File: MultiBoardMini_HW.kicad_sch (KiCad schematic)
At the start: 54 parts, among them J1 PB0, J2 PA10, J3 Conn_01x02_Male, J4 Conn_01x03, J6 Conn_01x04, SW1 PF1, SW2 RESET, SW3 PF0, SW4 PF1, T1 PTS_1.5_2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

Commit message: update sch
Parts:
- removed R11, R12: 10k, Resistor_SMD:R_0603_1608Metric, symbol Device:R
- SW4: value PF1 -> ~
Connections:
- net at ENC/IO_2.3 (Pin_3), PA2.2 (A), U2.4_7 (PA6): no longer IO_1.4 (Pin_4)
- net at J6.2 (Pin_2), U3.11 (RXD): now also U2.3_1 (PA9); no longer U2.4_5 (PA2)
- net at J6.1 (Pin_1), U3.12 (TXD): now also U2.3_2 (PA10); no longer U2.4_10 (PA3)
- net at SW3.2 (B): now also U2.4_15 (PB3); no longer U2.3_10 (PF0)
- net at U5.22 (PWM): now also U2.3_6 (PB0); no longer U2.3_1 (PA9)
- net at U2.3_12 (PA8): now also U5.8 (IN1); no longer U4.22 (PWM)
- net at U2.3_14 (PB5): now also U5.9 (IN2)
- net at U2.3_15 (PB4): now also U4.8 (IN1)
- net at J2.3 (Pin_3): now also U2.4_10 (PA3); no longer U2.3_2 (PA10)
- net at U2.3_7 (PB7): now also IO_1.4 (Pin_4); no longer U5.9 (IN2)
- net at U2.3_8 (PB6): now also IO_1.3 (Pin_3); no longer U5.8 (IN1)
- net at U2.3_9 (PB1): now also U4.22 (PWM); no longer U4.9 (IN2)
- net at U2.4_8 (PA5): now also U4.9 (IN2); no longer IO_1.3 (Pin_3)
- net at U2.4_9 (PA4): now also J1.3 (Pin_3)
- no-connect marks 8 -> 7
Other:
- moved on the sheet: J1, J2, PA1, PA2, PWR1, R4, R5, R6, SW3

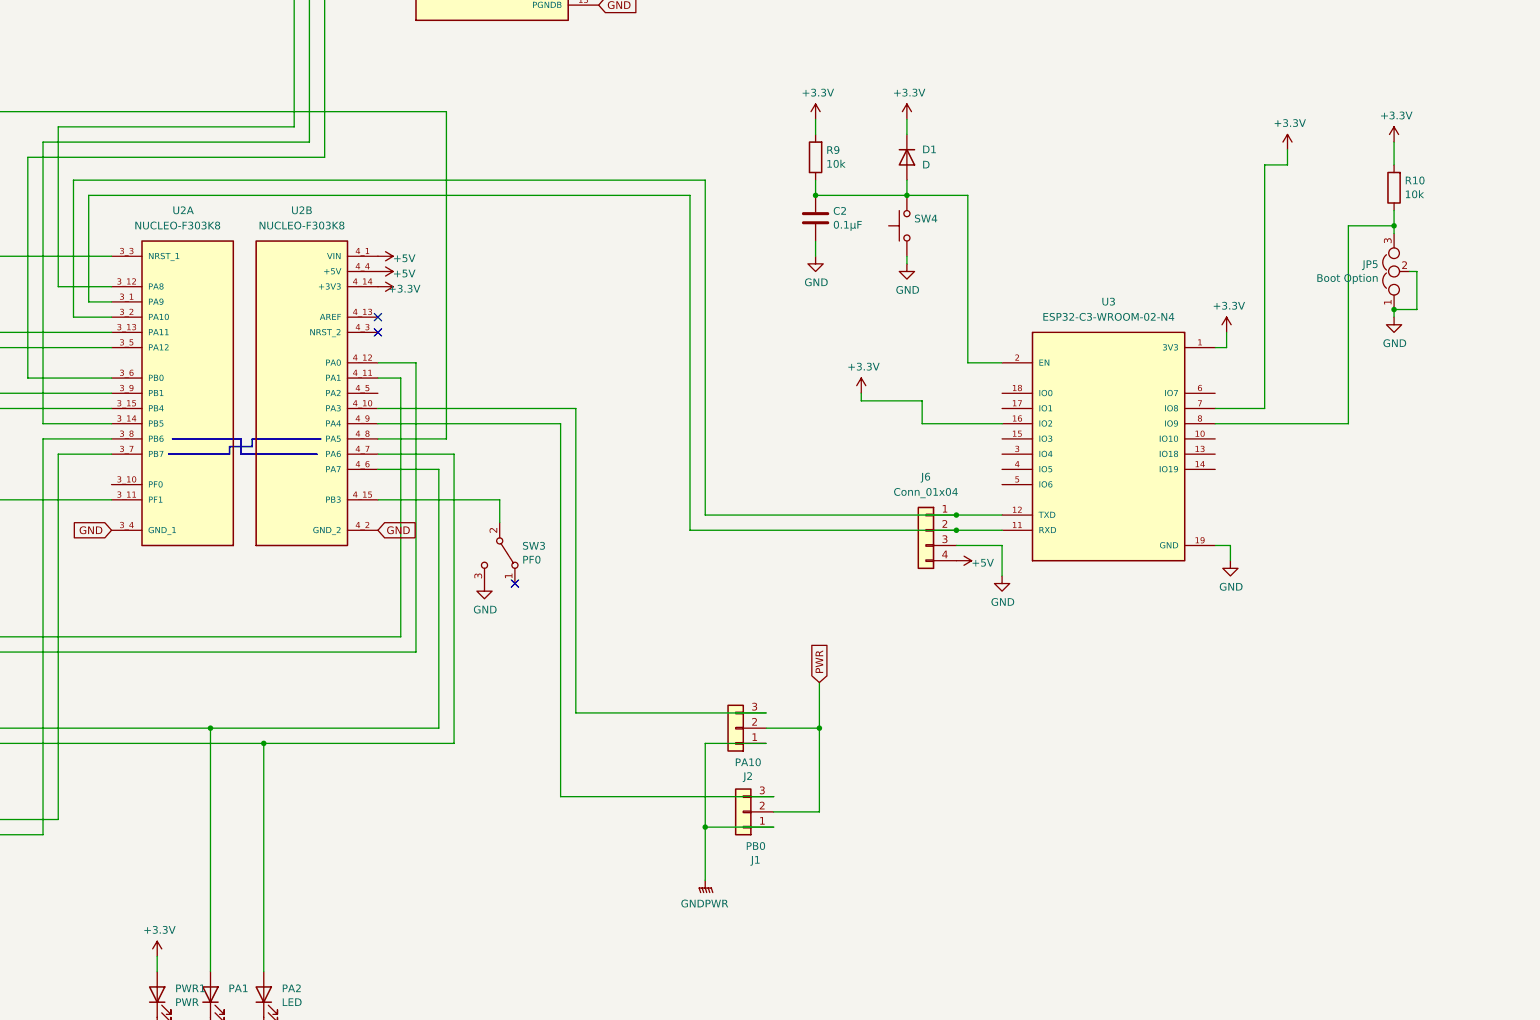
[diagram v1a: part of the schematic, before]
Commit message: add slide switch footprints
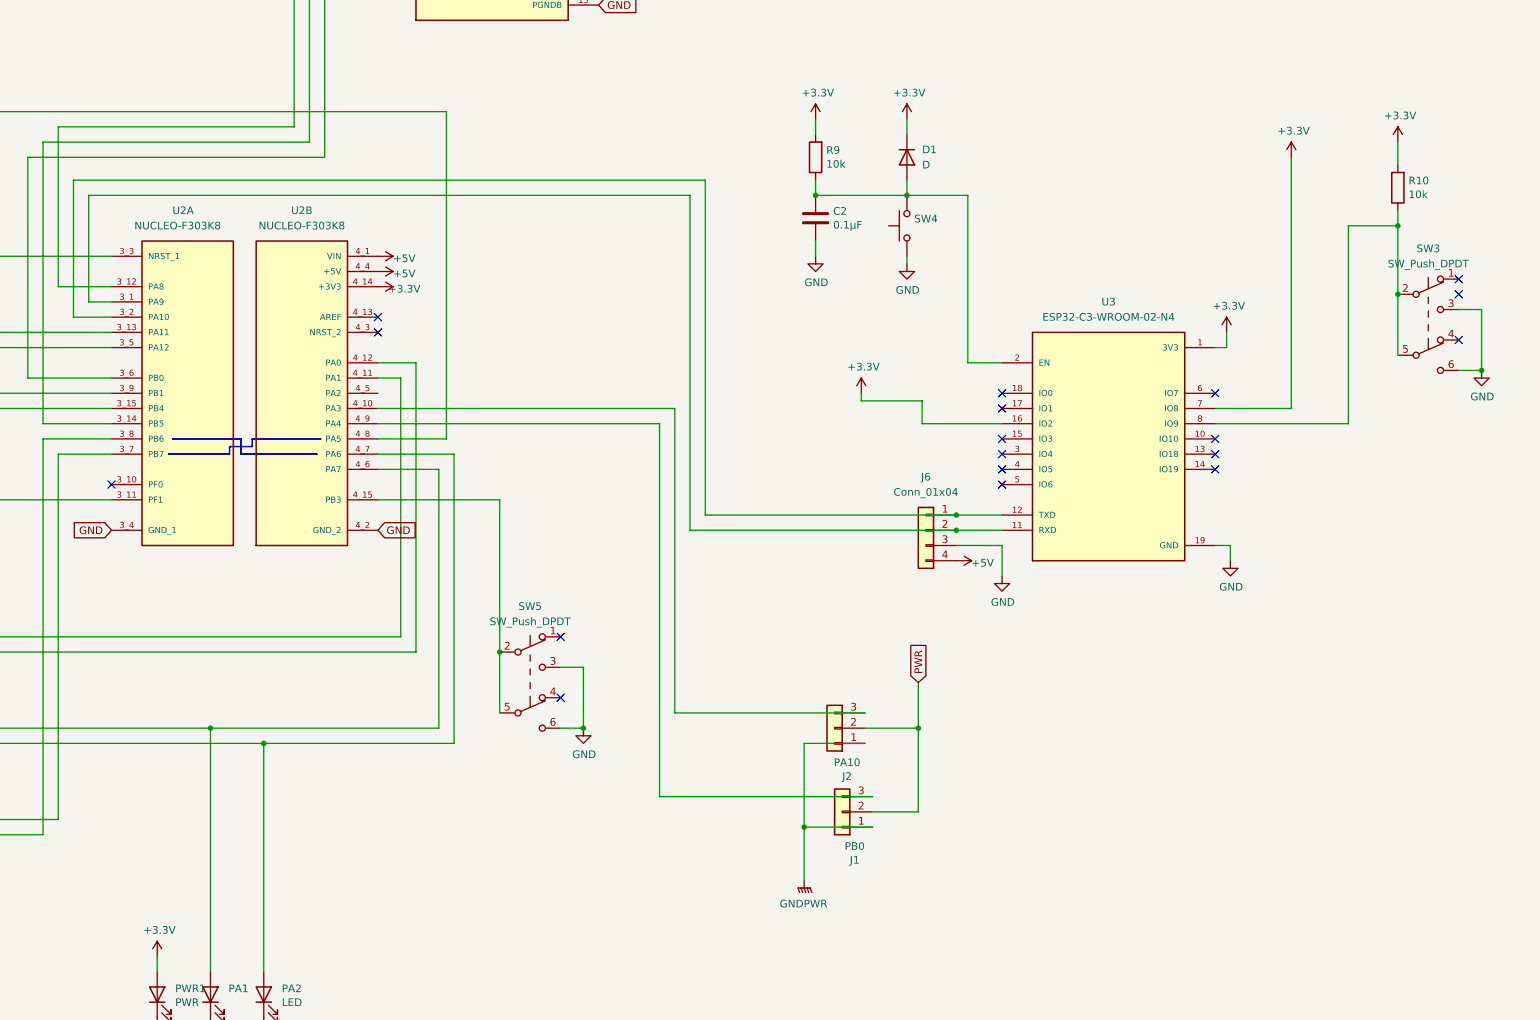
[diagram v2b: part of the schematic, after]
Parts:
- removed JP5: Boot Option, Jumper:SolderJumper-3_P2.0mm_Open_TrianglePad1.0x1.5mm, symbol Device:Jumper_NC_Dual
- removed SW3: PF0, IS-2235:IS-2235, symbol Switch:SW_SPDT
- added SW3, SW5: SW_Push_DPDT, MultiBoardMini_Libraries:SSSS213202, symbol Switch:SW_Push_DPDT
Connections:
- net GND: now also SW3.3 (C), SW3.6 (C), SW5.3 (C), SW5.6 (C)
- net at R10.1, U3.8 (IO9): now also SW3.2 (B), SW3.5 (B)
- net at U2.4_15 (PB3): now also SW5.2 (B), SW5.5 (B)
- no-connect marks 7 -> 22
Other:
- moved on the sheet: J1, J2, R10

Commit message: Update iroiro
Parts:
- removed J4: Conn_01x03, Connector_PinHeader_2.54mm:PinHeader_1x03_P2.54mm_Vertical, symbol Connector_Generic:Conn_01x03
- added J2: PA10, Connector_PinHeader_2.54mm:PinHeader_1x03_P2.54mm_Vertical, symbol Connector_Generic:Conn_01x03
- SW4: footprint Button_Switch_THT:SW_PUSH_6mm_H4.3mm -> Button_Switch_SMD:SW_Push_1P1T_NO_Vertical_Wuerth_434133025816
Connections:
- net +5V: now also J2.3 (Pin_3)
- net PWR: now also J2.2 (Pin_2)
- net at U3.1 (Vin): now also J2.1 (Pin_1)
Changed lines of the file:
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@@
+    )
+  )
+  (symbol (lib_id "Connector_Generic:Conn_01x03") (at 487.68 127 0) (mirror x) (unit 1)
+    (in_bom yes) (on_board yes) (dnp no)
+    (property "Reference" "J2" (at 485.5972 135.0518 0)
+      (effects (font (size 1.27 1.27)))
+    )
+    (property "Value" "PA10" (at 485.5972 132.7404 0)
+      (effects (font (size 1.27 1.27)))
+    )
+    (property "Footprint" "Connector_PinHeader_2.54mm:PinHeader_1x03_P2.54mm_Vertical" (at 487.68 127 0)
+      (effects (font (size 1.27 1.27)) hide)
+    )
+    (property "Datasheet" "~" (at 487.68 127 0)
+      (effects (font (size 1.27 1.27)) hide)
+    )
+    (pin "1")
+    (pin "2")
+    (pin "3")
+    (instances
+      (project "MultiBoardMini"
+        (path "/7b4d6a3e-dec4-4756-807e-679f9b6d01df"
+          (reference "J2") (unit 1)
+        )
+      )
+      (project "MultiBoardMini_HW"
+        (path "/f89d8039-fb4d-432a-bf6a-fadbc30a6f09"
+          (reference "J4") (unit 1)
+        )
+      )
     )
   )
@@
       (effects (font (size 1.27 1.27)) (justify right))
     )
-    (property "Footprint" "Button_Switch_THT:SW_PUSH_6mm_H4.3mm" (at 412.115 204.47 0)
+    (property "Footprint" "Button_Switch_SMD:SW_Push_1P1T_NO_Vertical_Wuerth_434133025816" (at 412.115 204.47 0)
       (effects (font (size 1.27 1.27)) hide)
     )
@@
         )
       )
-    )
-  )
-  (symbol (lib_id "Connector_Generic:Conn_01x03") (at 477.52 127 0) (mirror y) (unit 1)
-    (in_bom yes) (on_board no) (dnp no)
-    (property "Reference" "J4" (at 479.6028 118.9482 0)
-      (effects (font (size 1.27 1.27)))
-    )
-    (property "Value" "Conn_01x03" (at 479.6028 121.2596 0)
-      (effects (font (size 1.27 1.27)))
-    )
-    (property "Footprint" "Connector_PinHeader_2.54mm:PinHeader_1x03_P2.54mm_Vertical" (at 477.52 127 0)
-      (effects (font (size 1.27 1.27)) hide)
-    )
-    (property "Datasheet" "~" (at 477.52 127 0)
-      (effects (font (size 1.27 1.27)) hide)
-    )
-    (pin "1")
-    (pin "2")
-    (pin "3")
-    (instances
-      (project "MultiBoardMini"
-        (path "/7b4d6a3e-dec4-4756-807e-679f9b6d01df"
-          (reference "J4") (unit 1)
-        )
-      )
-      (project "MultiBoardMini_HW"
-        (path "/f89d8039-fb4d-432a-bf6a-fadbc30a6f09"
-          (reference "J4") (unit 1)
-        )
-      )
